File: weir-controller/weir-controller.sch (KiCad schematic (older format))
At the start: 5 parts

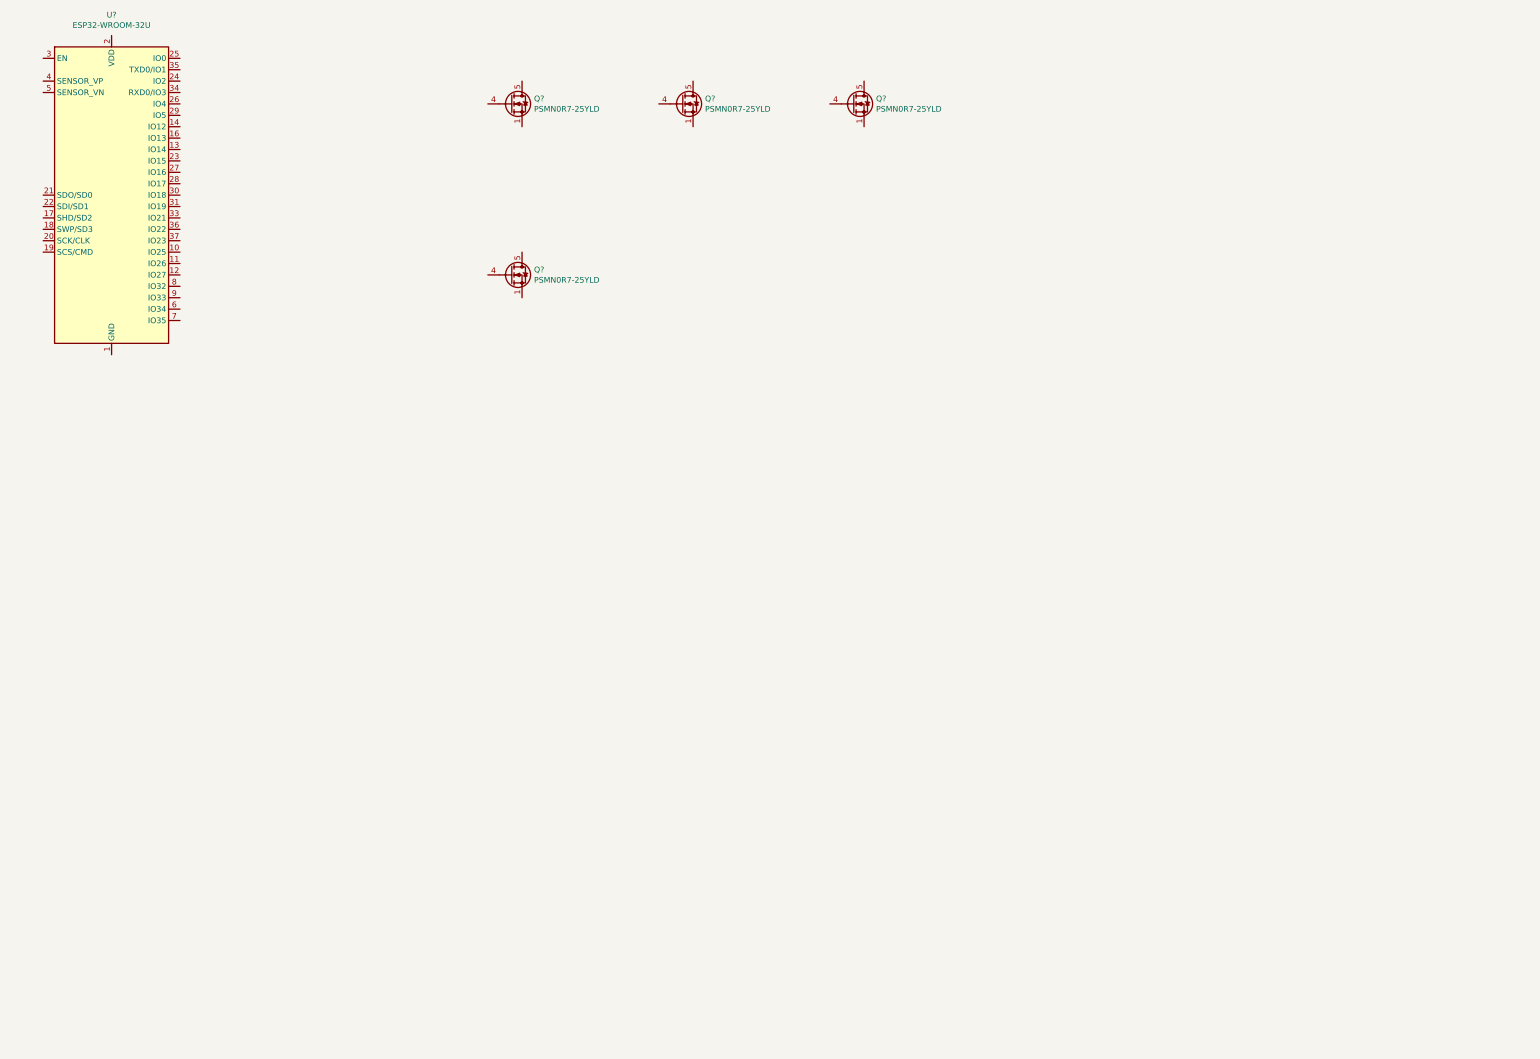
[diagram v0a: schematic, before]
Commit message: Move libs, inital rev of weir controller
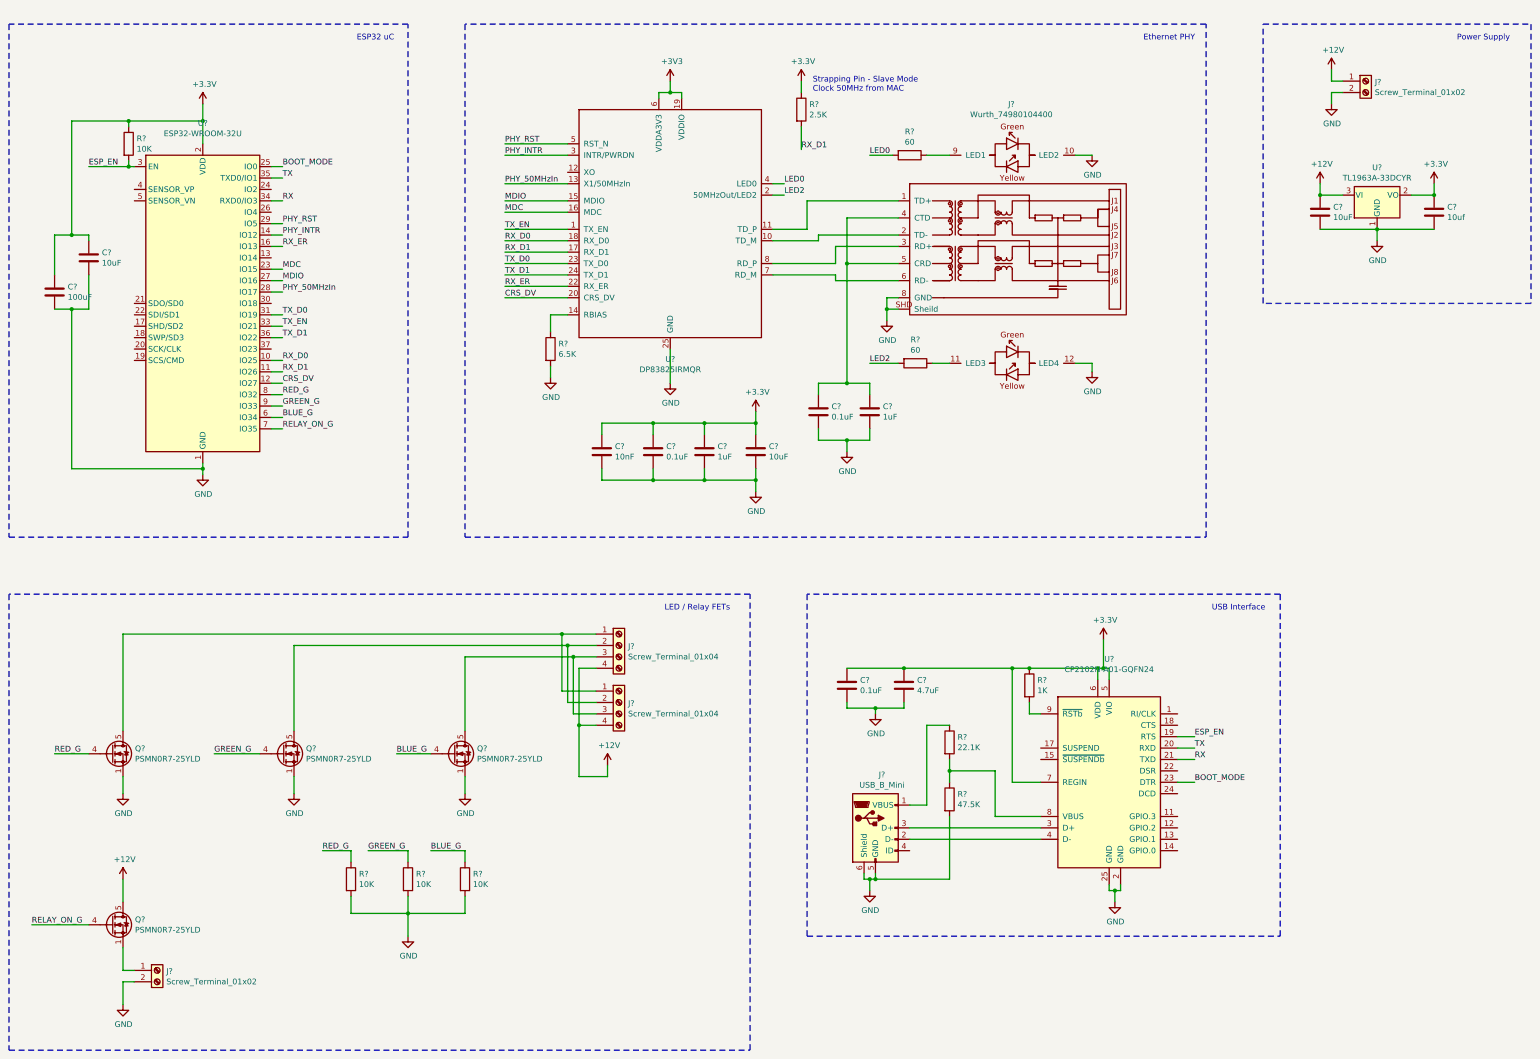
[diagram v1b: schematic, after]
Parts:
- added C? (x3): 10uF, symbol Device:C
- added C?: 10uf, symbol Device:C
- added C?: 4.7uF, symbol Device:C
- added C? (x3): 0.1uF, symbol Device:C
- added C?: 100uF, symbol Device:C
- added C?: 10nF, symbol Device:C
- added C? (x2): 1uF, symbol Device:C
- added J?: Wurth_74980104400, custom-parts:Wurth_74980104400, symbol custom-parts:Wurth_74980104400
- added J?: USB_B_Mini, custom-parts:54819-0589, symbol Connector:USB_B_Mini
- added J? (x2): Screw_Terminal_01x04, symbol Connector:Screw_Terminal_01x04
- added J? (x2): Screw_Terminal_01x02, symbol Connector:Screw_Terminal_01x02
- added R?: 22.1K, symbol Device:R
- added R?: 47.5K, symbol Device:R
- added R?: 1K, symbol Device:R
- added R? (x4): 10K, symbol Device:R
- added R?: 2.5K, symbol Device:R
- added R?: 6.5K, symbol Device:R
- added R? (x2): 60, symbol Device:R
- added U?: CP2102N-A01-GQFN24, Package_DFN_QFN:QFN-24-1EP_4x4mm_P0.5mm_EP2.6x2.6mm, symbol Interface_USB:CP2102N-A01-GQFN24
- added U?: DP83825IRMQR, Package_DFN_QFN:WQFN-24-1EP_4x4mm_P0.5mm_EP2.6x2.6mm, symbol custom-parts:DP83825IRMQR
- added U?: TL1963A-33DCYR, Package_TO_SOT_SMD:SOT-223-3_TabPin2, symbol Regulator_Linear:NCP1117-12_SOT223
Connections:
- net GND: now reaches U?.1 (GND), U?.15 (GND), U?.38 (GND), U?.39 (GND)
- net GND: now also Q?.1 (S), Q?.1 (S), Q?.1 (S), Q?.2 (S), Q?.2 (S), Q?.2 (S), Q?.3 (S), Q?.3 (S), Q?.3 (S), C?.2, C?.2, C?.2, C?.2, C?.2, C?.2, C?.2, C?.2, C?.2, C?.2, C?.2, C?.2, J?.10 (LED2), J?.12 (LED4), J?.2 (Pin_2), J?.2 (Pin_2), J?.5 (GND), J?.6 (Shield), J?.8 (GND), J?.SHD (Sheild), R?.2, R?.2, R?.2, R?.2, R?.2, U?.1 (GND), U?.2 (GND), U?.21 (GND), U?.25 (GND), U?.25 (GND), U?.9 (GND)
- net RX_D0: now reaches U?.10 (IO25)
- net RX_D0: now also U?.18 (RX_D0)
- net RX_D1: now reaches U?.11 (IO26)
- net RX_D1: now also R?.2, U?.17 (RX_D1)
- net CRS_DV: now reaches U?.12 (IO27)
- net CRS_DV: now also U?.20 (CRS_DV)
- net PHY_INTR: now reaches U?.14 (IO12)
- net PHY_INTR: now also U?.3 (INTR/PWRDN)
- net RX_ER: now reaches U?.16 (IO13)
- net RX_ER: now also U?.22 (RX_ER)
- net +3V3: now reaches U?.2 (VDD)
- net +3V3: now also C?.1, C?.1, C?.1, C?.1, C?.1, C?.1, C?.1, C?.1, C?.1, R?.1, R?.1, R?.1, U?.19 (VDDIO), U?.2 (VO), U?.5 (VIO), U?.6 (VDD), U?.6 (VDDA3V3), U?.7 (REGIN)
- net MDC: now reaches U?.23 (IO15)
- net MDC: now also U?.16 (MDC)
- net BOOT_MODE: now reaches U?.25 (IO0)
- net BOOT_MODE: now also U?.23 (DTR)
- net MDIO: now reaches U?.27 (IO16)
- net MDIO: now also U?.15 (MDIO)
- net PHY_50MHzIn: now reaches U?.28 (IO17)
- net PHY_50MHzIn: now also U?.13 (X1/50MHzIn)
- net PHY_RST: now reaches U?.29 (IO5)
- net PHY_RST: now also U?.5 (RST_N)
- net ESP_EN: now reaches U?.3 (EN)
- net ESP_EN: now also R?.2, U?.19 (RTS)
- net TX_D0: now reaches U?.31 (IO19)
- net TX_D0: now also U?.23 (TX_D0)
- net TX_EN: now reaches U?.33 (IO21)
- net TX_EN: now also U?.1 (TX_EN)
- net RX: now reaches U?.34 (RXD0/IO3)
- net RX: now also U?.21 (TXD)
- net TX: now reaches U?.35 (TXD0/IO1)
- net TX: now also U?.20 (RXD)
- net TX_D1: now reaches U?.36 (IO22)
- net TX_D1: now also U?.24 (TX_D1)
- net BLUE_G: now reaches U?.6 (IO34)
- net BLUE_G: now also Q?.4 (G), R?.1
- net RELAY_ON_G: now reaches U?.7 (IO35)
- net RELAY_ON_G: now also Q?.4 (G)
- net RED_G: now reaches U?.8 (IO32)
- net RED_G: now also Q?.4 (G), R?.1
- net GREEN_G: now reaches U?.9 (IO33)
- net GREEN_G: now also Q?.4 (G), R?.1
- net at Q?.5 (D): now also J?.1 (Pin_1), J?.1 (Pin_1)
- net at Q?.5 (D): now also J?.2 (Pin_2), J?.2 (Pin_2)
- net at Q?.5 (D): now also J?.3 (Pin_3), J?.3 (Pin_3)
- net at Q?.1 (S), Q?.2 (S), Q?.3 (S): now also J?.1 (Pin_1)
- net +12V: now reaches Q?.5 (D)
- net +12V: now also C?.1, J?.1 (Pin_1), J?.4 (Pin_4), J?.4 (Pin_4), U?.3 (VI)
- new net: J?.3 (D+), U?.3 (D+)
- new net: J?.2 (D-), U?.4 (D-)
- new net: R?.1, R?.2, U?.8 (VBUS)
- new net: R?.2, U?.9 (~RSTb)
- new net: J?.1 (TD+), U?.11 (TD_P)
- new net: J?.11 (LED3), R?.1
- new net: J?.2 (TD-), U?.10 (TD_M)
- new net: J?.3 (RD+), U?.8 (RD_P)
- new net: C?.1, C?.1, J?.4 (CTD), J?.5 (CRD)
- new net: J?.6 (RD-), U?.7 (RD_M)
- new net: J?.9 (LED1), R?.1
- new net: R?.1, U?.14 (RBIAS)
- new net: J?.1 (VBUS), R?.1
- new net LED0: R?.2, U?.4 (LED0)
- new net LED2: R?.2, U?.2 (50MHzOut/LED2)
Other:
- note added: "ESP32 uC"
- note added: "Ethernet PHY"
- note added: "LED / Relay FETs"
- note added: "Power Supply"
- note added: "Strapping Pin - Slave Mode\nClock 50MHz from MAC"
- note added: "USB Interface"
- moved on the sheet: Q?, U?

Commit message: Weir Controller v1.0
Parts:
- added R12: 10K, Resistor_SMD:R_0805_2012Metric_Pad1.15x1.40mm_HandSolder, symbol Device:R
- C1: renamed from C?; footprint (none) -> Capacitor_SMD:C_1206_3216Metric_Pad1.42x1.75mm_HandSolder
- C10, C11, C12, C2, C3, C4, C5, C6, C7, C8, C9: renamed from C?; footprint (none) -> Capacitor_SMD:C_0805_2012Metric_Pad1.15x1.40mm_HandSolder
- J1, J6: renamed from J?; footprint (none) -> custom-parts:PhoenixContact_PTSA_2Pin
- J2, J3: renamed from J?; footprint (none) -> custom-parts:PhoenixContact PTSA 4Pin
- R1, R10, R11, R2, R3, R4, R5, R6, R7, R8, R9: renamed from R?; footprint (none) -> Resistor_SMD:R_0805_2012Metric_Pad1.15x1.40mm_HandSolder
- U2: renamed from U?; footprint Package_DFN_QFN:WQFN-24-1EP_4x4mm_P0.5mm_EP2.6x2.6mm -> Package_DFN_QFN:WQFN-24-1EP_4x4mm_P0.5mm_EP2.6x2.6mm_ThermalVias
- U3: renamed from U?; footprint Package_DFN_QFN:QFN-24-1EP_4x4mm_P0.5mm_EP2.6x2.6mm -> Package_DFN_QFN:QFN-24-1EP_4x4mm_P0.5mm_EP2.6x2.6mm_ThermalVias
- gave numbers to parts that had none: 8
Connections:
- net +12V: now also J1.1 (Pin_1); no longer Q2.5 (D)
- net BLUE_G: now also U1.9 (IO33); no longer U1.6 (IO34)
- net GND: now also Q2.1 (S), Q2.2 (S), Q2.3 (S), R12.2; no longer J1.2 (Pin_2)
- net GREEN_G: now also U1.8 (IO32); no longer U1.9 (IO33)
- net RED_G: now also U1.7 (IO35); no longer U1.8 (IO32)
- net RELAY_ON_G: now also U1.6 (IO34), R12.1; no longer U1.7 (IO35)
- net USB_P: now reaches J4.3 (D+), U3.3 (D+)
- net USB_N: now reaches J4.2 (D-), U3.4 (D-)
- net TD_P: now reaches J5.1 (TD+), U2.11 (TD_P)
- net TD_N: now reaches J5.2 (TD-), U2.10 (TD_M)
- net RD_P: now reaches J5.3 (RD+), U2.8 (RD_P)
- net RD_N: now reaches J5.6 (RD-), U2.7 (RD_M)
- new net: J1.2 (Pin_2), Q2.5 (D)
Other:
- moved on the sheet: J1, Q2

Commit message: Fix a bunch of fuck ups
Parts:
- removed U4: TL1963A-33DCYR, Package_TO_SOT_SMD:SOT-223-3_TabPin2, symbol Regulator_Linear:NCP1117-12_SOT223
- added D1: LED_ABGR, LED_SMD:LED_Cree-PLCC4_2x2mm_CW, symbol custom-parts:LED_ABGR
- added R13: 80, Resistor_SMD:R_0805_2012Metric_Pad1.15x1.40mm_HandSolder, symbol Device:R
- added SW1: SW_Push, custom-parts:PTS636, symbol Switch:SW_Push
- added U4: TL1963A-33DCYR, Package_TO_SOT_SMD:SOT-223-3_TabPin2, symbol custom-parts:TL1963A-33DCYR
- J6: footprint custom-parts:PhoenixContact_PTSA_2Pin -> custom-parts:PhoenixContact_PTSA_2PIN_8A
- U2: footprint Package_DFN_QFN:WQFN-24-1EP_4x4mm_P0.5mm_EP2.6x2.6mm_ThermalVias -> custom-parts:TI_RMQ0024A
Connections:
- net +12V: now also U4.1 (IN)
- net +3V3: now also D1.1 (A), U4.3 (OUT)
- net GND: now also SW1.2, U4.2 (GND)
- net RED_G: now also U1.26 (IO4); no longer U1.7 (IO35)
- net RELAY_ON_G: now also U1.24 (IO2); no longer U1.6 (IO34)
- net IND_R: now reaches U1.13 (IO14)
- net IND_R: now also R13.2
- net IND_G: now reaches U1.30 (IO18)
- net IND_G: now also D1.3 (GK)
- net IND_B: now reaches U1.37 (IO23)
- net IND_B: now also D1.2 (BK)
- net RED_CATHODE: now reaches J2.1 (Pin_1), J3.1 (Pin_1), Q1.5 (D)
- net GREEN_CATHODE: now reaches J2.2 (Pin_2), J3.2 (Pin_2), Q3.5 (D)
- net BLUE_CATHODE: now reaches J2.3 (Pin_3), J3.3 (Pin_3), Q4.5 (D)
- net RELAY_NEGATIVE: now reaches J1.2 (Pin_2), Q2.5 (D)
- new net: D1.4 (RK), R13.1
- new net FACTORY_RESET: SW1.1, U1.7 (IO35)
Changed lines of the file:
@@
-$EndComp
-$Comp
-L Regulator_Linear:NCP1117-12_SOT223 U4
-U 1 1 5E9CE6A1
-P 13000 2500
-F 0 "U4" H 13000 2742 50  0000 C CNN
-F 1 "TL1963A-33DCYR" H 13000 2651 50  0000 C CNN
-F 2 "Package_TO_SOT_SMD:SOT-223-3_TabPin2" H 13000 2700 50  0001 C CNN
-F 3 "http://www.onsemi.com/pub_link/Collateral/NCP1117-D.PDF" H 13100 2250 50  0001 C CNN
-	1    13000 2500
-	1    0    0    -1
 $EndComp
 $Comp
@@
 F 0 "J6" H 12980 1492 50  0000 L CNN
 F 1 "Screw_Terminal_01x02" H 12980 1401 50  0000 L CNN
-F 2 "custom-parts:PhoenixContact_PTSA_2Pin" H 12900 1500 50  0001 C CNN
+F 2 "custom-parts:PhoenixContact_PTSA_2PIN_8A" H 12900 1500 50  0001 C CNN
 F 3 "~" H 12900 1500 50  0001 C CNN
 	1    12900 1500
@@
 	1    0    0    -1
 $EndComp
-Connection ~ 13500 2500
-Connection ~ 12500 2500
-Wire Wire Line
-	13300 2500 13500 2500
 Wire Wire Line
 	12500 2800 13000 2800
@@
 Wire Wire Line
 	13000 2800 13500 2800
-Wire Wire Line
-	12500 2500 12700 2500
 Wire Wire Line
 	10050 8150 8900 8150
@@
 Wire Wire Line
 	1700 3500 1550 3500
-Text Label 3400 4450 0    50   ~ 0
+Text Label 3400 2450 0    50   ~ 0
 RELAY_ON_G
 Text Label 3400 4350 0    50   ~ 0
@@
 Text Label 3400 4250 0    50   ~ 0
 GREEN_G
-Text Label 3400 4550 0    50   ~ 0
+Text Label 3400 2650 0    50   ~ 0
 RED_G
 Wire Wire Line
@@
 Wire Wire Line
 	3300 4350 3400 4350
-Wire Wire Line
-	3300 4450 3400 4450
-Wire Wire Line
-	3300 4550 3400 4550
 Text Label 5350 2050 0    50   ~ 0
 PHY_RST
@@
 F 0 "U2" H 6800 1561 50  0000 C CNN
 F 1 "DP83825IRMQR" H 6800 1470 50  0000 C CNN
-F 2 "Package_DFN_QFN:WQFN-24-1EP_4x4mm_P0.5mm_EP2.6x2.6mm_ThermalVias" H 6750 1350 50  0001 C CNN
+F 2 "custom-parts:TI_RMQ0024A" H 6750 1350 50  0001 C CNN
 F 3 "" H 6500 3050 50  0001 C CNN
 	1    6800 2750
@@
 Text Label 9400 8150 0    50   ~ 0
 USB_N
+$Comp
+L custom-parts:TL1963A-33DCYR U4
+U 1 1 5EBD715B
+P 13000 2550
+F 0 "U4" H 13000 2865 50  0000 C CNN
+F 1 "TL1963A-33DCYR" H 13000 2774 50  0000 C CNN
+F 2 "Package_TO_SOT_SMD:SOT-223-3_TabPin2" H 13000 2550 50  0001 C CNN
+F 3 "http://www.ti.com/lit/ds/symlink/tl1963a.pdf" H 13000 2550 50  0001 C CNN
+	1    13000 2550
+	1    0    0    -1
+$EndComp
+Wire Wire Line
+	12500 2500 12700 2500
+Connection ~ 12500 2500
+Wire Wire Line
+	13300 2500 13500 2500
+Connection ~ 13500 2500
+Wire Wire Line
+	3300 2450 3400 2450
+Wire Wire Line
+	3300 2650 3400 2650
+Wire Wire Line
+	3300 4550 3550 4550
+Wire Wire Line
+	3550 4550 3550 4950
+Wire Wire Line
+	3550 4950 3750 4950
+$Comp
+L power:GND #PWR0101
+U 1 1 5EC66C12
+P 4250 5050
+F 0 "#PWR0101" H 4250 4800 50  0001 C CNN
+F 1 "GND" H 4255 4877 50  0000 C CNN
+F 2 "" H 4250 5050 50  0001 C CNN
+F 3 "" H 4250 5050 50  0001 C CNN
+	1    4250 5050
+	1    0    0    -1
+$EndComp
+Wire Wire Line
+	4150 4950 4250 4950
+Wire Wire Line
+	4250 4950 4250 5050
+$Comp
+L Switch:SW_Push SW1
+U 1 1 5EC87E21
+P 3950 4950
+F 0 "SW1" H 3950 5235 50  0000 C CNN
+F 1 "SW_Push" H 3950 5144 50  0000 C CNN
+F 2 "custom-parts:PTS636" H 3950 5150 50  0001 C CNN
+F 3 "~" H 3950 5150 50  0001 C CNN
+	1    3950 4950
+	1    0    0    -1
+$EndComp
+Text Label 3550 4550 0    50   ~ 0
+FACTORY_RESET
+$Comp
+L custom-parts:LED_ABGR D1
+U 1 1 5ECC3E30
+P 3900 1700
+F 0 "D1" H 3900 2197 50  0000 C CNN
+F 1 "LED_ABGR" H 3900 2106 50  0000 C CNN
+F 2 "LED_SMD:LED_Cree-PLCC4_2x2mm_CW" H 3900 1700 50  0001 C CNN
+F 3 "~" H 3900 1700 50  0001 C CNN
+	1    3900 1700
+	1    0    0    -1
+$EndComp
+Text Label 3250 1500 0    50   ~ 0
+IND_G
+Text Label 3100 1700 0    50   ~ 0
+IND_R
+Text Label 3250 1900 0    50   ~ 0
+IND_B
+$Comp
+L Device:R R13
+U 1 1 5ECCB9D4
+P 3500 1700
+F 0 "R13" V 3293 1700 50  0000 C CNN
+F 1 "80" V 3384 1700 50  0000 C CNN
+F 2 "Resistor_SMD:R_0805_2012Metric_Pad1.15x1.40mm_HandSolder" V 3430 1700 50  0001 C CNN
+F 3 "~" H 3500 1700 50  0001 C CNN
+	1    3500 1700
+	0    1    1    0
+$EndComp
+Wire Wire Line
+	3700 1700 3650 1700
+Wire Wire Line
+	3700 1500 3250 1500
+Wire Wire Line
+	3100 1700 3350 1700
+Wire Wire Line
+	3700 1900 3250 1900
+$Comp
+L power:+3.3V #PWR0102
+U 1 1 5ED1FFEA
+P 4250 1600
+F 0 "#PWR0102" H 4250 1450 50  0001 C CNN
+F 1 "+3.3V" H 4265 1773 50  0000 C CNN
+F 2 "" H 4250 1600 50  0001 C CNN
+F 3 "" H 4250 1600 50  0001 C CNN
+	1    4250 1600
+	1    0    0    -1
+$EndComp
+Wire Wire Line
+	4250 1600 4250 1700
+Wire Wire Line
+	4250 1700 4100 1700
+Text Label 3400 3050 0    50   ~ 0
+IND_R
+Text Label 3400 3450 0    50   ~ 0
+IND_G
+Text Label 3400 3850 0    50   ~ 0
+IND_B
+Wire Wire Line
+	3300 3850 3400 3850
+Wire Wire Line
+	3300 3450 3400 3450
+Wire Wire Line
+	3300 3050 3400 3050
+Text Label 2000 6900 0    50   ~ 0
+RED_CATHODE
+Text Label 3500 6900 0    50   ~ 0
+GREEN_CATHODE
+Text Label 5000 6900 0    50   ~ 0
+BLUE_CATHODE
+Text Label 2000 9000 0    50   ~ 0
+RELAY_NEGATIVE
 $EndSCHEMATC

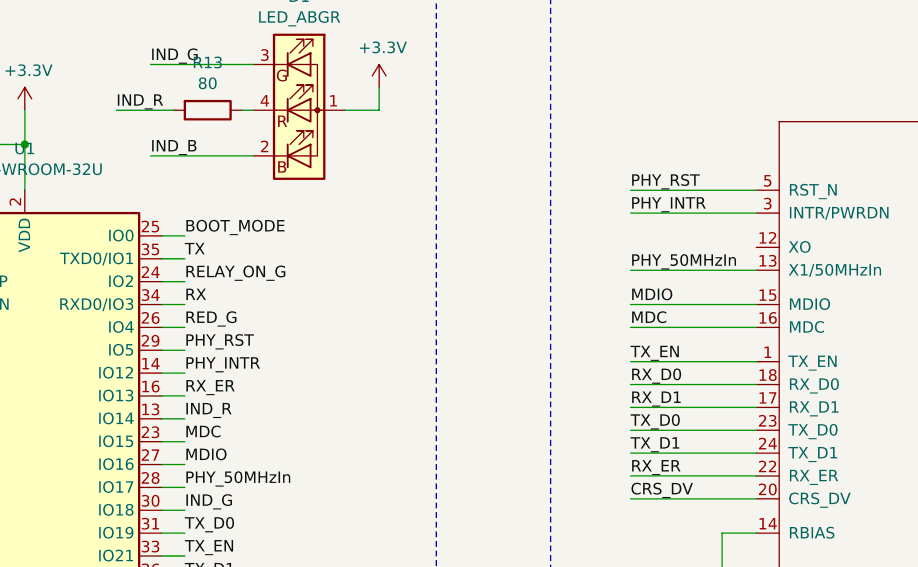
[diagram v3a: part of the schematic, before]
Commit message: Remove phy interrupt
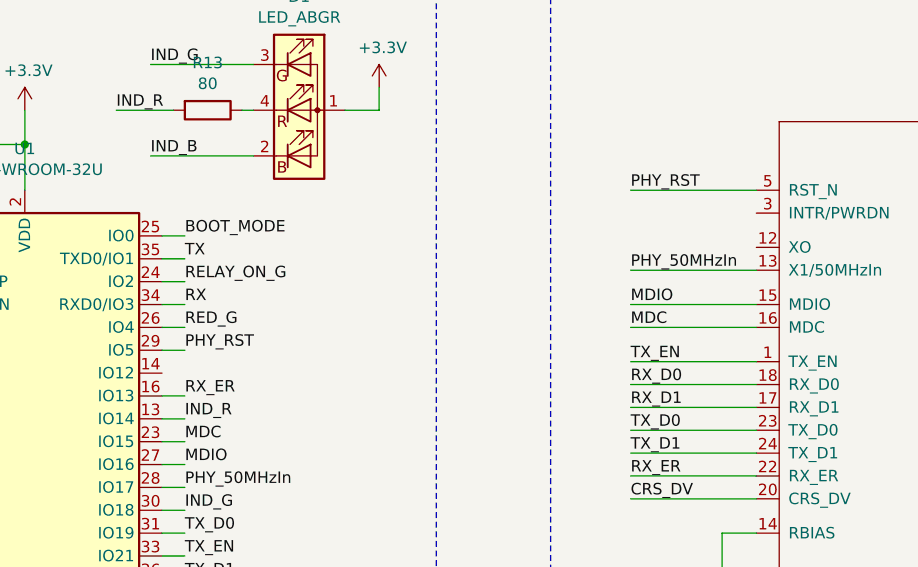
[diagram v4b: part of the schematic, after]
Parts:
- U1: footprint RF_Module:ESP32-WROOM-32U -> custom-parts:ESP32-WROOM-32U
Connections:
- net PHY_INTR: no longer names the net of U1.14 (IO12)
- net PHY_INTR: no longer U2.3 (INTR/PWRDN)
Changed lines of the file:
@@
 F 0 "U1" H 2700 5031 50  0000 C CNN
 F 1 "ESP32-WROOM-32U" H 2700 4940 50  0000 C CNN
-F 2 "RF_Module:ESP32-WROOM-32U" H 2700 1950 50  0001 C CNN
+F 2 "custom-parts:ESP32-WROOM-32U" H 2700 1950 50  0001 C CNN
 F 3 "https://www.espressif.com/sites/default/files/documentation/esp32-wroom-32d_esp32-wroom-32u_datasheet_en.pdf" H 2400 3500 50  0001 C CNN
 	1    2700 3450
@@
 Text Label 5350 2050 0    50   ~ 0
 PHY_RST
-Text Label 5350 2150 0    50   ~ 0
-PHY_INTR
 Text Label 5350 2400 0    50   ~ 0
 PHY_50MHzIn
@@
 CRS_DV
 Wire Wire Line
-	5350 2150 5900 2150
-Wire Wire Line
 	5350 2400 5900 2400
 Wire Wire Line
@@
 Text Label 3400 2750 0    50   ~ 0
 PHY_RST
-Text Label 3400 2850 0    50   ~ 0
-PHY_INTR
 Wire Wire Line
 	3300 2750 3400 2750
-Wire Wire Line
-	3300 2850 3400 2850
 $Comp
 L custom-parts:DP83825IRMQR U2

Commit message: v1.1.1
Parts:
- added R14, R15, R16, R17, R18, R19, R20: 33, Resistor_SMD:R_0805_2012Metric_Pad1.15x1.40mm_HandSolder, symbol Device:R
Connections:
- net CRS_DV: now also R19.2; no longer U2.20 (CRS_DV)
- net PHY_50MHzIn: now also R20.1; no longer U1.28 (IO17)
- net RX_D0: now also R17.1; no longer U2.18 (RX_D0)
- net RX_D1: now also R18.2; no longer R6.2, U2.17 (RX_D1)
- net TX_D0: now also R16.2; no longer U1.31 (IO19)
- net TX_D1: now also R14.1; no longer U1.36 (IO22)
- net TX_EN: now also R15.2; no longer U1.33 (IO21)
- new net: R20.2, U1.28 (IO17)
- new net: R16.1, U1.31 (IO19)
- new net: R15.1, U1.33 (IO21)
- new net: R14.2, U1.36 (IO22)
- new net: R17.2, U2.18 (RX_D0)
- new net: R19.1, U2.20 (CRS_DV)
- new net RX_D1_M: R18.1, R6.2, U2.17 (RX_D1)
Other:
- moved on the sheet: C1, C2, C3, C4, C5, C6, C7, C9, D1, J5, R1, R13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
